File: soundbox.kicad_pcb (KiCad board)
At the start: 2 copper layers, 28 x 24.5 mm, 2 parts, among them J1 MICRO_SD_CARD_HOLDER, P1 CONN_01X10

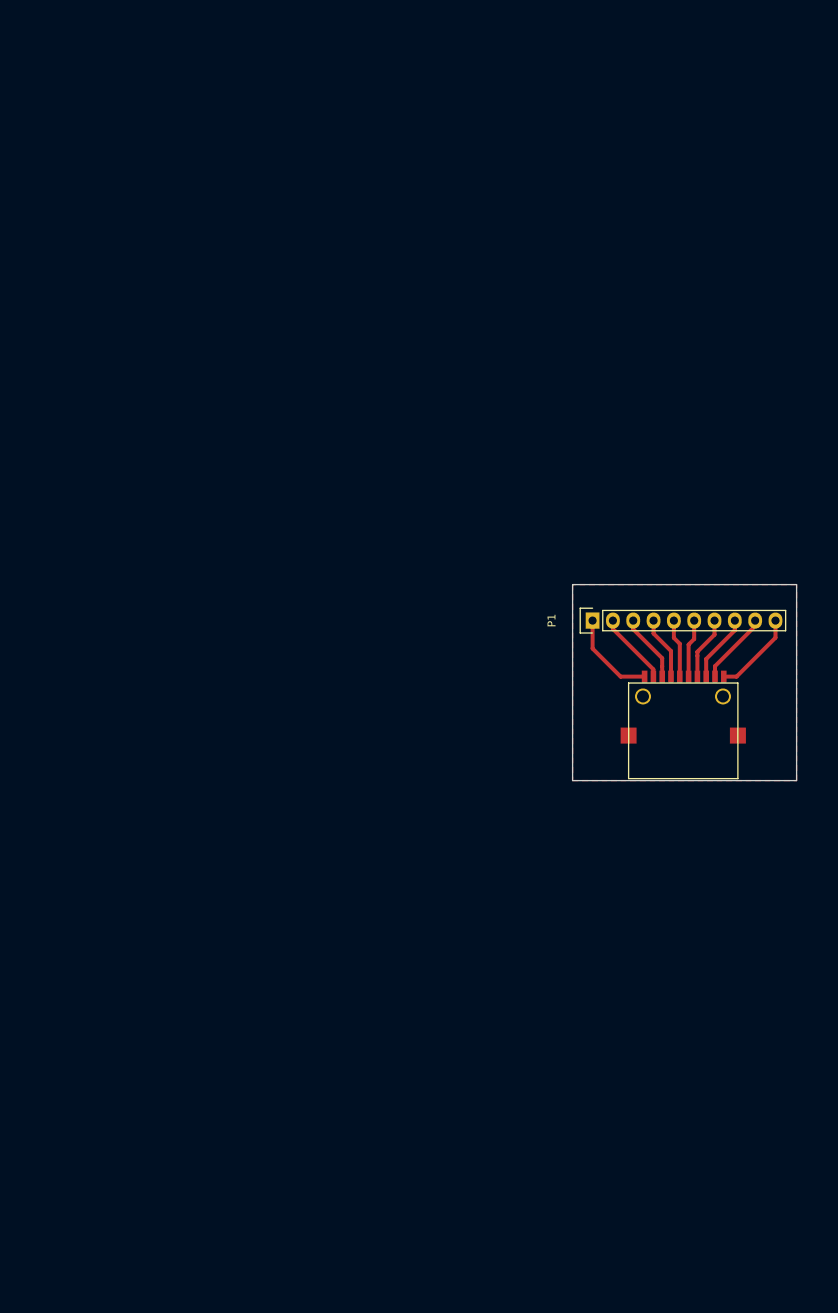
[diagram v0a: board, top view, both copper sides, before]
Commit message: final version of schematic packages assigned raw placement on layout
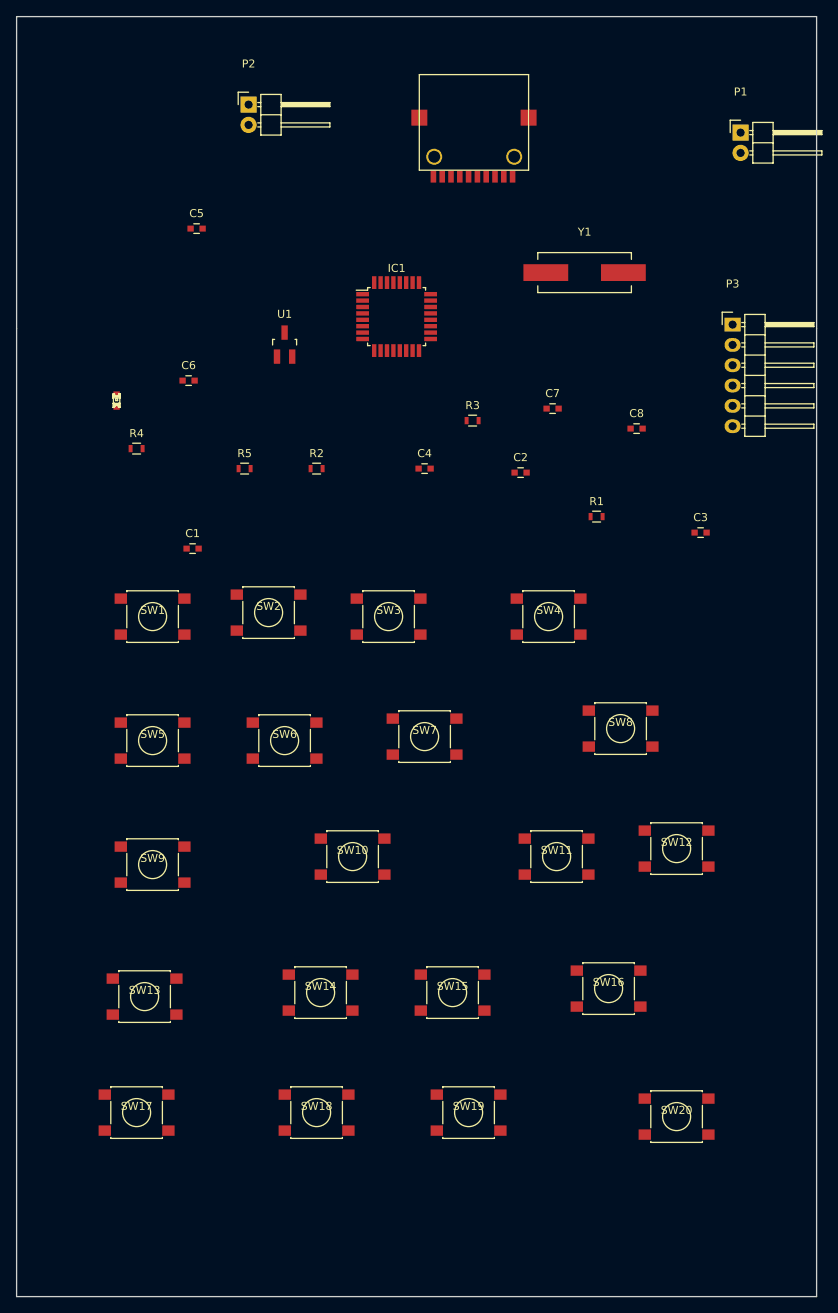
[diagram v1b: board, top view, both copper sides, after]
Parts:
- added C1: 100n, Capacitors_SMD:C_0603, F.Cu at (92.0, 89.0)
- added C2: 100n, Capacitors_SMD:C_0603, F.Cu at (133.0, 79.5)
- added C3: 100n, Capacitors_SMD:C_0603, F.Cu at (155.5, 87.0)
- added C4: 100n, Capacitors_SMD:C_0603, F.Cu at (121.0, 79.0)
- added C5: 100n, Capacitors_SMD:C_0603, F.Cu at (92.5, 49.0)
- added C6: 23p, Capacitors_SMD:C_0603, F.Cu at (91.5, 68.0)
- added C7: 23p, Capacitors_SMD:C_0603, F.Cu at (137.0, 71.5)
- added C8: 100n, Capacitors_SMD:C_0603, F.Cu at (147.5, 74.0)
- added D1: LED, led:led-CHIPLED_0603, F.Cu at (82.5, 70.5)
- added IC1: ATMEGA328-A, Housings_QFP:TQFP-32_7x7mm_Pitch0.8mm, F.Cu at (117.5, 60.0)
- added P2: CONN_01X02, Pin_Headers:Pin_Header_Angled_1x02, F.Cu at (99.0, 33.5)
- added P3: CONN_01X06, Pin_Headers:Pin_Header_Angled_1x06, F.Cu at (159.5, 61.0)
- added R1: 220R, Resistors_SMD:R_0603, F.Cu at (142.5, 85.0)
- added R2: 0R, Resistors_SMD:R_0603, F.Cu at (107.5, 79.0)
- added R3: 1M, Resistors_SMD:R_0603, F.Cu at (127.0, 73.0)
- added R4: 15k, Resistors_SMD:R_0603, F.Cu at (85.0, 76.5)
- added R5: 1M, Resistors_SMD:R_0603, F.Cu at (98.5, 79.0)
- added SW1: SW_PUSH, Buttons_Switches_SMD:SW_SPST_PTS645, F.Cu at (87.0, 97.5)
- added SW10: SW_PUSH, Buttons_Switches_SMD:SW_SPST_PTS645, F.Cu at (112.0, 127.5)
- added SW11: SW_PUSH, Buttons_Switches_SMD:SW_SPST_PTS645, F.Cu at (137.5, 127.5)
- added SW12: SW_PUSH, Buttons_Switches_SMD:SW_SPST_PTS645, F.Cu at (152.5, 126.5)
- added SW13: SW_PUSH, Buttons_Switches_SMD:SW_SPST_PTS645, F.Cu at (86.0, 145.0)
- added SW14: SW_PUSH, Buttons_Switches_SMD:SW_SPST_PTS645, F.Cu at (108.0, 144.5)
- added SW15: SW_PUSH, Buttons_Switches_SMD:SW_SPST_PTS645, F.Cu at (124.5, 144.5)
- added SW16: SW_PUSH, Buttons_Switches_SMD:SW_SPST_PTS645, F.Cu at (144.0, 144.0)
- added SW17: SW_PUSH, Buttons_Switches_SMD:SW_SPST_PTS645, F.Cu at (85.0, 159.5)
- added SW18: SW_PUSH, Buttons_Switches_SMD:SW_SPST_PTS645, F.Cu at (107.5, 159.5)
- added SW19: SW_PUSH, Buttons_Switches_SMD:SW_SPST_PTS645, F.Cu at (126.5, 159.5)
- added SW2: SW_PUSH, Buttons_Switches_SMD:SW_SPST_PTS645, F.Cu at (101.5, 97.0)
- added SW20: SW_PUSH, Buttons_Switches_SMD:SW_SPST_PTS645, F.Cu at (152.5, 160.0)
- added SW3: SW_PUSH, Buttons_Switches_SMD:SW_SPST_PTS645, F.Cu at (116.5, 97.5)
- added SW4: SW_PUSH, Buttons_Switches_SMD:SW_SPST_PTS645, F.Cu at (136.5, 97.5)
- added SW5: SW_PUSH, Buttons_Switches_SMD:SW_SPST_PTS645, F.Cu at (87.0, 113.0)
- added SW6: SW_PUSH, Buttons_Switches_SMD:SW_SPST_PTS645, F.Cu at (103.5, 113.0)
- added SW7: SW_PUSH, Buttons_Switches_SMD:SW_SPST_PTS645, F.Cu at (121.0, 112.5)
- added SW8: SW_PUSH, Buttons_Switches_SMD:SW_SPST_PTS645, F.Cu at (145.5, 111.5)
- added SW9: SW_PUSH, Buttons_Switches_SMD:SW_SPST_PTS645, F.Cu at (87.0, 128.5)
- added U1: MCP1700, TO_SOT_Packages_SMD:SOT-23_Handsoldering, F.Cu at (103.5, 63.5)
- added Y1: 16MHz, Crystals:Crystal_HC49-SD_SMD, F.Cu at (141.0, 54.5)
- J1: value MICRO_SD_CARD_HOLDER -> µSD
- P1: value CONN_01X10 -> CONN_01X02; footprint Pin_Headers:Pin_Header_Straight_1x10 -> Pin_Headers:Pin_Header_Angled_1x02
- moved J1 64.6 mm to (132.0, 42.5), turned to 180 degrees
- moved P1 63.7 mm to (160.5, 37.0), turned to 0 degrees
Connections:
- J1 pad : Net-(J1-Pad6) -> (no net)
- J1 pad 10: Net-(J1-Pad10) -> GND
- J1 pad 2: Net-(J1-Pad2) -> /CS
- J1 pad 3: Net-(J1-Pad3) -> /MOSI
- J1 pad 4: Net-(J1-Pad4) -> +3V3
- J1 pad 5: Net-(J1-Pad5) -> /SCK
- J1 pad 6: Net-(J1-Pad6) -> GND
- J1 pad 7: Net-(J1-Pad7) -> /MISO
- J1 pad 9: Net-(J1-Pad9) -> /SD_SW
- P1 pad 1: Net-(J1-Pad1) -> +12V
- P1 pad 2: Net-(J1-Pad2) -> GND
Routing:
- net Net-(J1-Pad1): track 11.5 -> 0.00 mm
- net Net-(J1-Pad10): track 10.6 -> 0.00 mm
- net Net-(J1-Pad2): track 9.10 -> 0.00 mm
- net Net-(J1-Pad9): track 9.08 -> 0.00 mm
- net Net-(J1-Pad3): track 8.50 -> 0.00 mm
- net Net-(J1-Pad8): track 8.49 -> 0.00 mm
- net Net-(J1-Pad4): track 7.91 -> 0.00 mm
- net Net-(J1-Pad7): track 7.89 -> 0.00 mm
- net Net-(J1-Pad5): track 7.31 -> 0.00 mm
- net Net-(J1-Pad6): track 7.29 -> 0.00 mm
- removed copper zone on F.Cu, net Net-(J1-Pad6)
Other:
- board size 28 x 24.5 mm -> 100 x 160 mm
